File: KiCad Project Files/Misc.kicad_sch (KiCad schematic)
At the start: 19 parts, among them J2 SWD, U5 74AHCT1G125

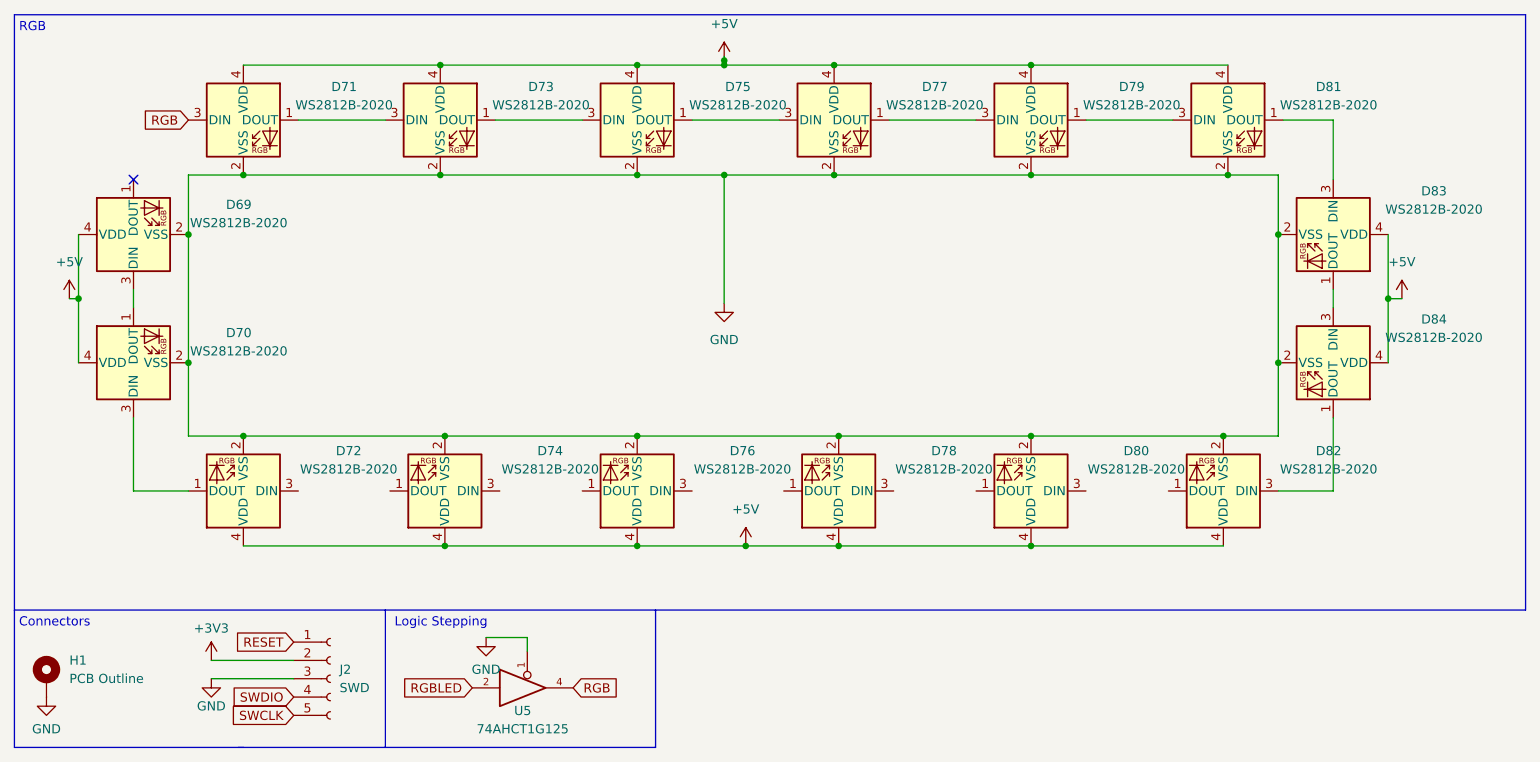
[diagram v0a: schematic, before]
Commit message: Initial Modifications
Summary of changes from original SST60:
-Removes extraneous keys, opting for ANSI-only, split right shift, split Backspace, 7U space bar, stepped caps lock.
-Switched from MX-ANSI hybrid to MX-only
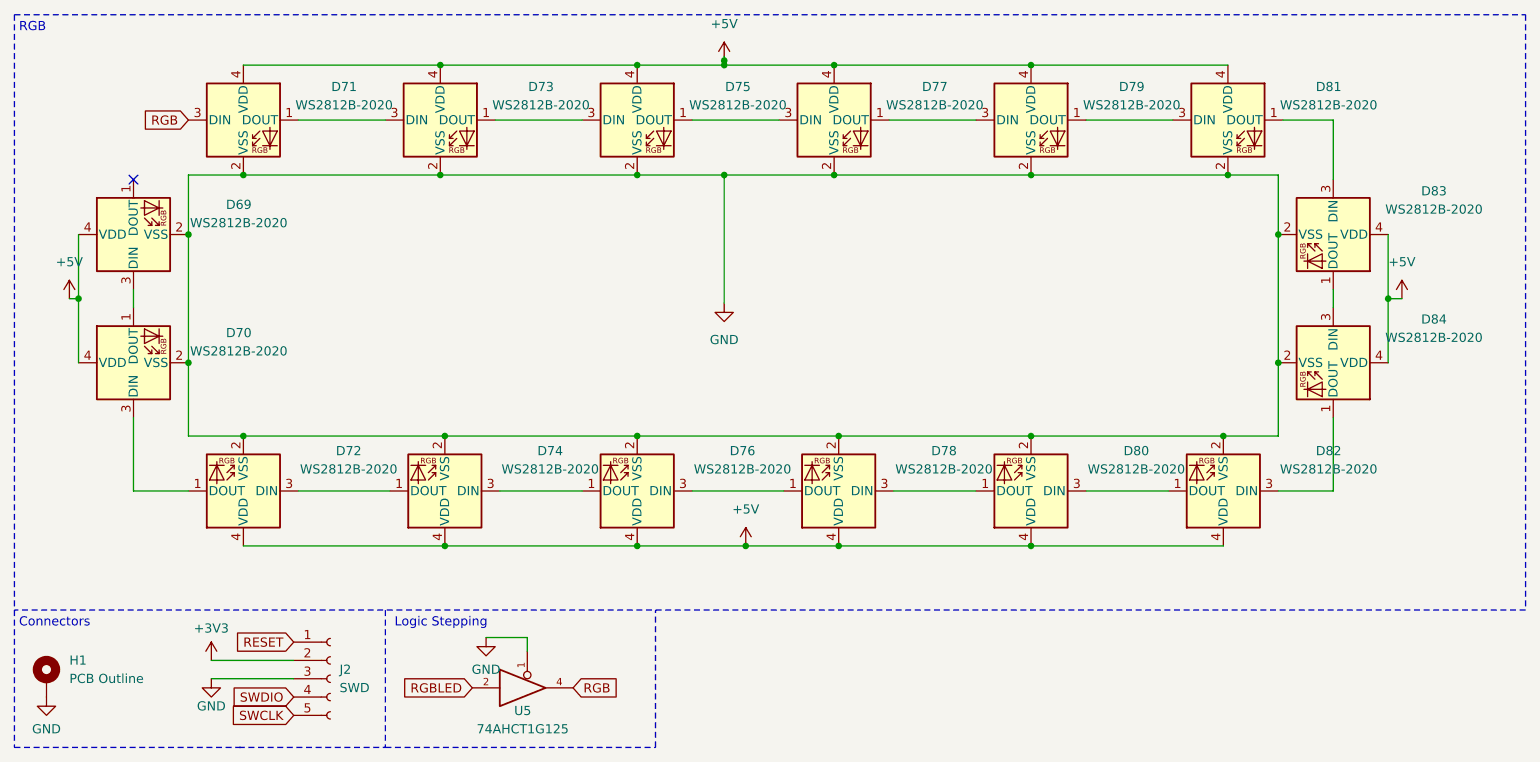
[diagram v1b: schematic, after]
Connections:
- net at D74.1 (DOUT): now also D72.3 (DIN)
- net at D74.3 (DIN): now also D76.1 (DOUT)
- net at D76.3 (DIN): now also D78.1 (DOUT)
- net at D82.1 (DOUT): now also D80.3 (DIN)
- net at D80.1 (DOUT): now also D78.3 (DIN)

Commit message: Further Component Updates
More updating of components to decide what is and isn't included in output BOM and Placement files, as well as other component values, to smooth out wrinkles with JLC PCB process.
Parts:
- H1, J2: now left out of the parts list
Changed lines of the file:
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@@
 		(unit 1)
 		(exclude_from_sim no)
-		(in_bom yes)
+		(in_bom no)
 		(on_board yes)
 		(dnp no)
@@
 		(unit 1)
 		(exclude_from_sim no)
-		(in_bom yes)
-		(on_board yes)
-		(dnp no)
+		(in_bom no)
+		(on_board yes)
+		(dnp no)
